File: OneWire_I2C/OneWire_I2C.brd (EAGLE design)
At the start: 22.2 x 28.2 mm, 14 parts, among them Q1 TP0602N3

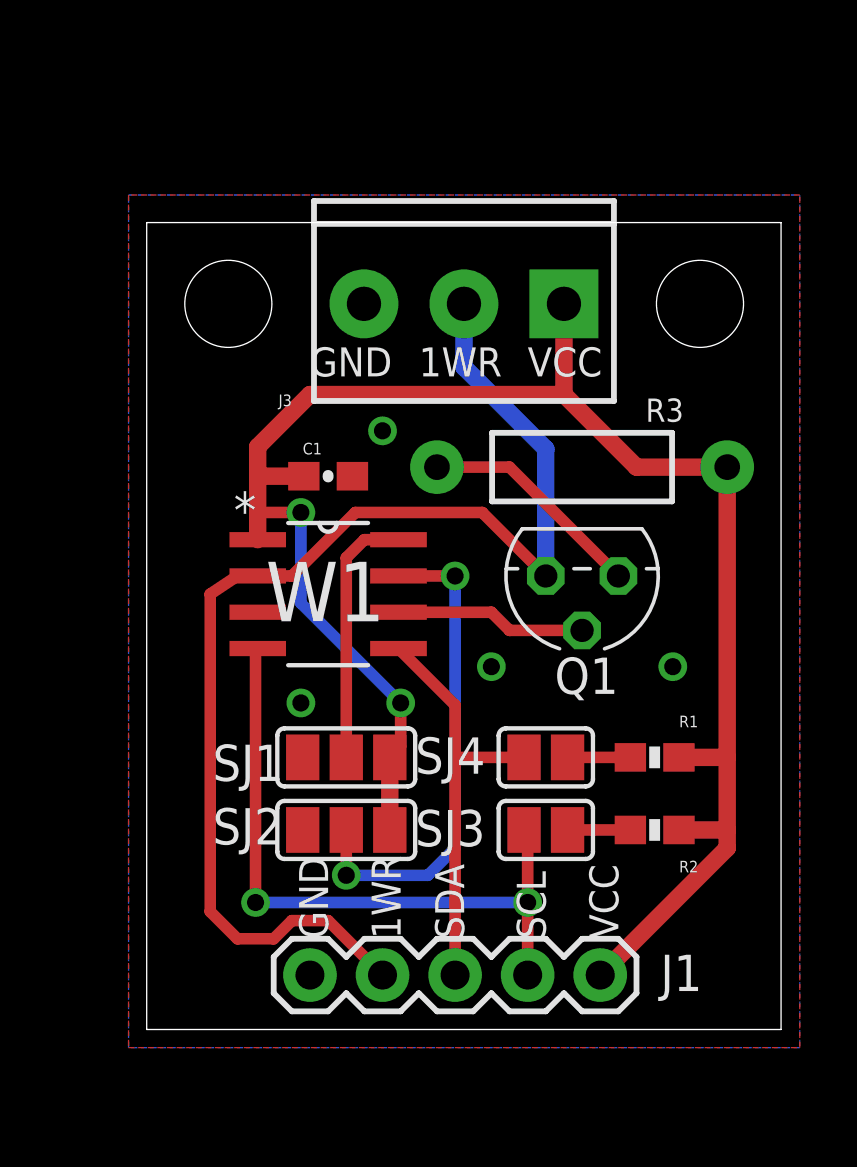
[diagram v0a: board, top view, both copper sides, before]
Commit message: Tweaks to I2C 1Wire bridge boards
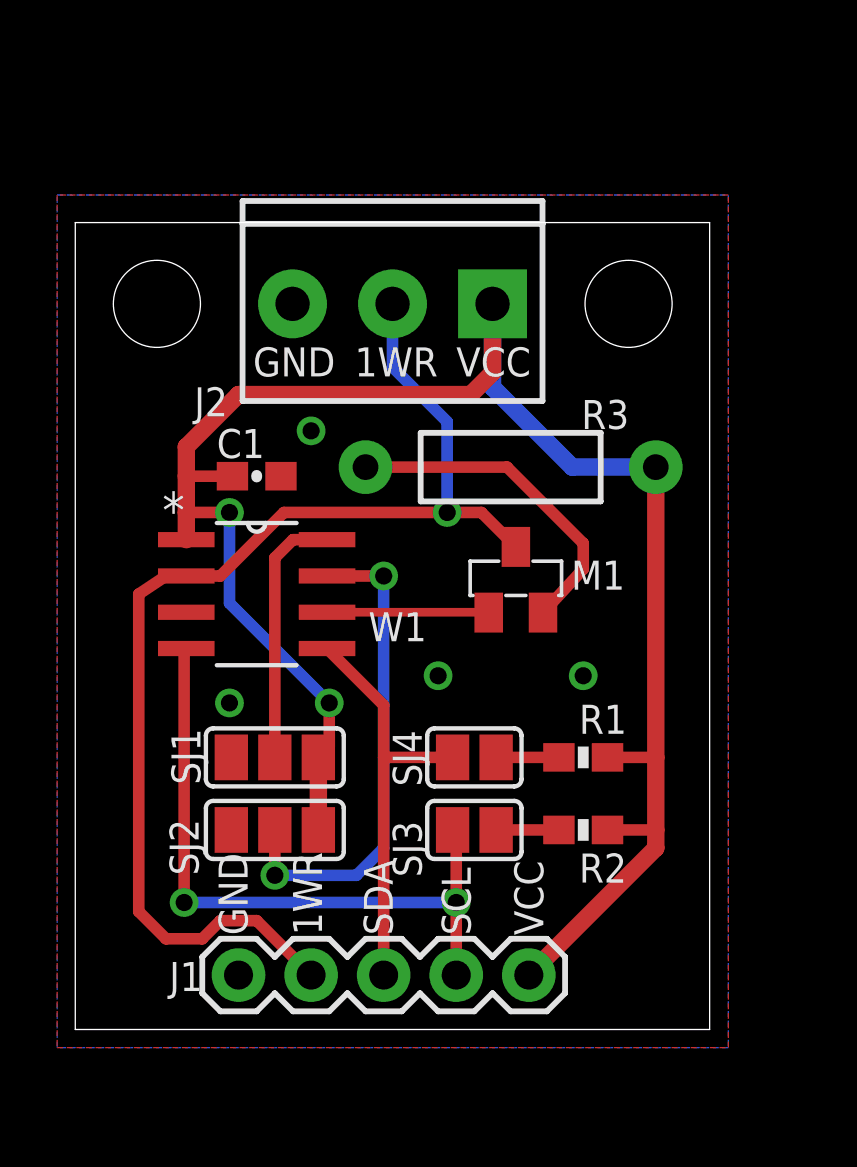
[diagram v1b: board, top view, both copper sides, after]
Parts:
- removed J3: (no value), SparkFun-Connectors:SCREWTERMINAL-3.5MM-3
- removed Q1: TP0602N3, transistor-fet:TO-92
- added J2: (no value), SparkFun-Connectors:SCREWTERMINAL-3.5MM-3
- added M1: BSS84, Puffin:SOT-23
- moved R3 2.50 mm to (15.3, 19.7)
- moved SJ3 2.50 mm to (14.0, 6.99)
- moved SJ4 2.50 mm to (14.0, 9.53)
- moved C1 2.50 mm to (6.39, 19.4)
- moved W1 2.50 mm to (6.39, 15.2)
- moved J1 2.50 mm to (15.9, 1.91)
- moved R1 2.50 mm to (17.8, 9.53)
- moved R2 2.50 mm to (17.8, 6.99)
- moved SJ1 2.50 mm to (7.03, 9.53)
- moved SJ2 2.50 mm to (7.03, 6.99)
- moved U$1 2.50 mm to (2.90, 25.4)
- moved U$2 2.50 mm to (19.4, 25.4)
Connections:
- removed net PCTL: Q1.2, W1.6
- new net N$1: M1.1, W1.6
- net 1WR: now also J2.2, M1.3; no longer J3.2, Q1.3
- net GND: now also J2.3; no longer J3.3
- net N$10: now also M1.2; no longer Q1.1
- net VCC: now also J2.1; no longer J3.1
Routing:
- net PCTL: track 6.69 -> 0.00 mm
- net N$1: track 0.00 -> 5.67 mm
- net N$10: track 7.93 -> 11.7 mm
- net VCC: track 63.5 -> 66.1 mm
- net 1WR: track 42.4 -> 40.8 mm, vias 0 -> 1

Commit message: Changed I2C pullup jumpers to single 3-way jumper
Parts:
- removed SJ4: (no value), jumper:SJ
- SJ3: device jumper:SJ -> jumper:SJ_2
- moved SJ3 4.74 mm to (18.5, 8.50), turned to 90 degrees
- moved R2 3.54 mm to (14.3, 7.49)
- moved R1 3.50 mm to (14.3, 9.53)
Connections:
- removed net N$4: R1.2, SJ4.2
- new net N$2: R1.1, SJ3.3
- net N$3: now also R2.1, SJ3.1; no longer R2.2, SJ3.2
- net SCL: now also R2.2; no longer SJ3.1
- net SDA: now also R1.2; no longer SJ4.1
- net VCC: now also SJ3.2; no longer R1.1, R2.1
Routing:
- net N$2: track 0.00 -> 3.56 mm
- net N$4: track 2.20 -> 0.00 mm
- net N$3: track 2.20 -> 3.54 mm
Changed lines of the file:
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@@
 <setting verticaltext="up"/>
 </settings>
-<grid distance="0.5" unitdist="mm" unit="mm" style="dots" multiple="1" display="yes" altdistance="0.1" altunitdist="mm" altunit="mm"/>
+<grid distance="0.01" unitdist="inch" unit="inch" style="dots" multiple="1" display="yes" altdistance="0.005" altunitdist="inch" altunit="inch"/>
 <layers>
-<layer number="1" name="Top" color="4" fill="1" visible="no" active="yes"/>
+<layer number="1" name="Top" color="4" fill="1" visible="yes" active="yes"/>
 <layer number="2" name="Route2" color="1" fill="3" visible="no" active="no"/>
 <layer number="3" name="Route3" color="4" fill="3" visible="no" active="no"/>
@@
 <attribute name="VALUE" x="5.374" y="18.2245" size="0.4064" layer="27" font="vector"/>
 </element>
-<element name="R1" library="SparkFun-Resistors" package="0603-RES" value="" x="17.82" y="9.525" smashed="yes" rot="R180">
-<attribute name="NAME" x="19.344" y="11.3665" size="1.016" layer="25" font="vector" ratio="15" rot="R180"/>
-<attribute name="VALUE" x="18.836" y="10.668" size="0.4064" layer="27" font="vector" rot="R180"/>
-</element>
-<element name="R2" library="SparkFun-Resistors" package="0603-RES" value="" x="17.82" y="6.985" smashed="yes" rot="R180">
-<attribute name="NAME" x="19.344" y="6.1595" size="1.016" layer="25" font="vector" ratio="15" rot="R180"/>
-<attribute name="VALUE" x="18.836" y="8.128" size="0.4064" layer="27" font="vector" rot="R180"/>
-</element>
-<element name="SJ3" library="jumper" package="SJ" value="" x="14.01" y="6.985" smashed="yes">
-<attribute name="NAME" x="12.1685" y="5.334" size="1.016" layer="25" font="vector" ratio="15" rot="R90"/>
-<attribute name="VALUE" x="14.4101" y="6.985" size="0.02" layer="27"/>
-</element>
-<element name="SJ4" library="jumper" package="SJ" value="" x="14.01" y="9.525" smashed="yes">
-<attribute name="NAME" x="12.1685" y="8.509" size="1.016" layer="25" font="vector" ratio="15" rot="R90"/>
-<attribute name="VALUE" x="14.4101" y="9.525" size="0.02" layer="27"/>
+<element name="R1" library="SparkFun-Resistors" package="0603-RES" value="" x="14.32" y="9.525" smashed="yes" rot="R180">
+<attribute name="NAME" x="12.844" y="10.1665" size="1.016" layer="25" font="vector" ratio="15" rot="R180"/>
+<attribute name="VALUE" x="15.336" y="10.668" size="0.4064" layer="27" font="vector" rot="R180"/>
+</element>
+<element name="R2" library="SparkFun-Resistors" package="0603-RES" value="" x="14.32" y="7.485" smashed="yes" rot="R180">
+<attribute name="NAME" x="12.744" y="8.1595" size="1.016" layer="25" font="vector" ratio="15" rot="R180"/>
+<attribute name="VALUE" x="15.336" y="8.628" size="0.4064" layer="27" font="vector" rot="R180"/>
 </element>
 <element name="SJ2" library="jumper" package="SJ_2" value="" x="7.025" y="6.985" smashed="yes" rot="R180">
@@
 <attribute name="NAME" x="17.3995" y="15.3955" size="1.016" layer="25" font="vector" ratio="15"/>
 </element>
+<element name="SJ3" library="jumper" package="SJ_2" value="" x="18.5" y="8.5" smashed="yes" rot="R90">
+<attribute name="NAME" x="20.73" y="7.325" size="1.016" layer="25" font="vector" ratio="15" rot="R90"/>
+<attribute name="VALUE" x="18.5" y="8.3999" size="0.02" layer="27" rot="R90"/>
+</element>
 </elements>
 <signals>
 <signal name="VCC">
-<contactref element="R1" pad="1"/>
-<contactref element="R2" pad="1"/>
 <contactref element="W1" pad="1"/>
 <contactref element="C1" pad="1"/>
@@
 <contactref element="J1" pad="1"/>
 <contactref element="J2" pad="1"/>
-<wire x1="15.915" y1="1.905" x2="20.36" y2="6.35" width="0.6096" layer="1"/>
-<wire x1="20.36" y1="6.35" x2="20.36" y2="6.985" width="0.6096" layer="1"/>
-<wire x1="20.36" y1="6.985" x2="20.36" y2="9.525" width="0.6096" layer="1"/>
-<wire x1="20.36" y1="9.525" x2="20.36" y2="19.685" width="0.6096" layer="1"/>
-<wire x1="18.67" y1="9.525" x2="20.36" y2="9.525" width="0.4064" layer="1"/>
-<wire x1="18.67" y1="6.985" x2="20.36" y2="6.985" width="0.4064" layer="1"/>
-<wire x1="3.9262" y1="17.145" x2="3.9262" y2="18.0975" width="0.6096" layer="1"/>
-<wire x1="3.9262" y1="18.0975" x2="3.9262" y2="19.3675" width="0.6096" layer="1"/>
+<wire x1="20.36" y1="4.35" x2="20.36" y2="8.5" width="0.6096" layer="1"/>
+<wire x1="20.36" y1="8.5" x2="20.36" y2="19.685" width="0.6096" layer="1"/>
+<wire x1="3.9262" y1="17.145" x2="3.9262" y2="19.3675" width="0.6096" layer="1"/>
 <wire x1="3.9262" y1="19.3675" x2="3.9262" y2="20.3962" width="0.6096" layer="1"/>
 <wire x1="3.9262" y1="20.3962" x2="5.755" y2="22.225" width="0.6096" layer="1"/>
@@
 <wire x1="8.93" y1="9.906" x2="8.93" y2="11.43" width="0.4064" layer="1"/>
 <via x="8.93" y="11.43" extent="1-16" drill="0.6"/>
-<wire x1="8.93" y1="11.43" x2="5.4375" y2="14.9225" width="0.4064" layer="16"/>
-<wire x1="5.4375" y1="14.9225" x2="5.4375" y2="18.0975" width="0.4064" layer="16"/>
-<via x="5.4375" y="18.0975" extent="1-16" drill="0.6"/>
-<wire x1="5.4375" y1="18.0975" x2="3.9262" y2="18.0975" width="0.4064" layer="1"/>
+<wire x1="8.93" y1="11.43" x2="3.9135" y2="16.4465" width="0.4064" layer="16"/>
+<wire x1="3.9135" y1="16.4465" x2="3.9135" y2="19.3675" width="0.4064" layer="16"/>
+<via x="3.9135" y="19.3675" extent="1-16" drill="0.6"/>
 <wire x1="20.36" y1="19.685" x2="17.439" y2="19.685" width="0.6096" layer="16"/>
 <wire x1="17.439" y1="19.685" x2="14.645" y2="22.479" width="0.6096" layer="16"/>
@@
 <wire x1="13.883" y1="22.225" x2="14.645" y2="22.987" width="0.6096" layer="1"/>
 <wire x1="14.645" y1="22.987" x2="14.645" y2="25.4" width="0.6096" layer="1"/>
+<contactref element="SJ3" pad="2"/>
+<wire x1="18.5" y1="8.5" x2="20.36" y2="8.5" width="0.4064" layer="1"/>
+<wire x1="20.36" y1="4.35" x2="20.35" y2="4.35" width="0.6096" layer="1"/>
+<wire x1="20.35" y1="4.35" x2="18" y2="2" width="0.6096" layer="1"/>
+<wire x1="18" y1="2" x2="16.01" y2="2" width="0.6096" layer="1"/>
+<wire x1="16.01" y1="2" x2="15.915" y2="1.905" width="0.6096" layer="1"/>
+<wire x1="3.9135" y1="19.3675" x2="3.9262" y2="19.3675" width="0" layer="19" extent="1-1"/>
 </signal>
 <signal name="GND">
@@
 <via x="5.4375" y="11.43" extent="1-16" drill="0.6"/>
 </signal>
-<signal name="N$3">
-<contactref element="SJ3" pad="2"/>
-<contactref element="R2" pad="2"/>
-<wire x1="14.772" y1="6.985" x2="16.97" y2="6.985" width="0.4064" layer="1"/>
-</signal>
-<signal name="N$4">
-<contactref element="SJ4" pad="2"/>
-<contactref element="R1" pad="2"/>
-<wire x1="14.772" y1="9.525" x2="16.97" y2="9.525" width="0.4064" layer="1"/>
-</signal>
 <signal name="SCL">
 <contactref element="W1" pad="4"/>
-<contactref element="SJ3" pad="1"/>
 <contactref element="J1" pad="2"/>
 <wire x1="3.9262" y1="13.335" x2="3.85" y2="13.335" width="0.4064" layer="1"/>
@@
 <via x="13.375" y="4.445" extent="1-16" drill="0.6"/>
 <wire x1="13.375" y1="4.445" x2="13.375" y2="1.905" width="0.4064" layer="1"/>
-<wire x1="13.248" y1="6.985" x2="13.375" y2="6.985" width="0.4064" layer="1"/>
 <wire x1="13.375" y1="6.985" x2="13.375" y2="4.445" width="0.4064" layer="1"/>
+<contactref element="R2" pad="2"/>
+<wire x1="13.375" y1="6.985" x2="13.47" y2="7.485" width="0" layer="19" extent="1-1"/>
 </signal>
 <signal name="AD1">
@@
 <signal name="SDA">
 <contactref element="W1" pad="5"/>
-<contactref element="SJ4" pad="1"/>
 <contactref element="J1" pad="3"/>
-<wire x1="10.835" y1="1.905" x2="10.835" y2="9.525" width="0.4064" layer="1"/>
+<wire x1="10.835" y1="1.905" x2="10.835" y2="9.5" width="0.4064" layer="1"/>
 <wire x1="10.835" y1="9.525" x2="10.835" y2="11.3538" width="0.4064" layer="1"/>
 <wire x1="10.835" y1="11.3538" x2="8.8538" y2="13.335" width="0.4064" layer="1"/>
-<wire x1="13.248" y1="9.525" x2="10.835" y2="9.525" width="0.4064" layer="1"/>
+<contactref element="R1" pad="2"/>
+<wire x1="13.47" y1="9.525" x2="10.835" y2="9.525" width="0.4064" layer="1"/>
+<wire x1="10.835" y1="9.525" x2="10.835" y2="9.5" width="0.4064" layer="1"/>
 </signal>
 <signal name="1WR">
@@
 <wire x1="14.5125" y1="14.605" x2="14.5125" y2="14.5925" width="0.4064" layer="1"/>
 </signal>
+<signal name="N$2">
+<contactref element="R1" pad="1"/>
+<contactref element="SJ3" pad="3"/>
+<wire x1="18.5" y1="10.024" x2="17.024" y2="10.024" width="0.4064" layer="1"/>
+<wire x1="17.024" y1="10.024" x2="16.5" y2="9.5" width="0.4064" layer="1"/>
+<wire x1="16.5" y1="9.5" x2="15.195" y2="9.5" width="0.4064" layer="1"/>
+<wire x1="15.195" y1="9.5" x2="15.17" y2="9.525" width="0.4064" layer="1"/>
+</signal>
+<signal name="N$3">
+<contactref element="R2" pad="1"/>
+<contactref element="SJ3" pad="1"/>
+<wire x1="15.17" y1="7.485" x2="16.515" y2="7.485" width="0.4064" layer="1"/>
+<wire x1="16.515" y1="7.485" x2="17" y2="7" width="0.4064" layer="1"/>
+<wire x1="17" y1="7" x2="18.476" y2="7" width="0.4064" layer="1"/>
+<wire x1="18.476" y1="7" x2="18.5" y2="6.976" width="0.4064" layer="1"/>
+</signal>
 </signals>

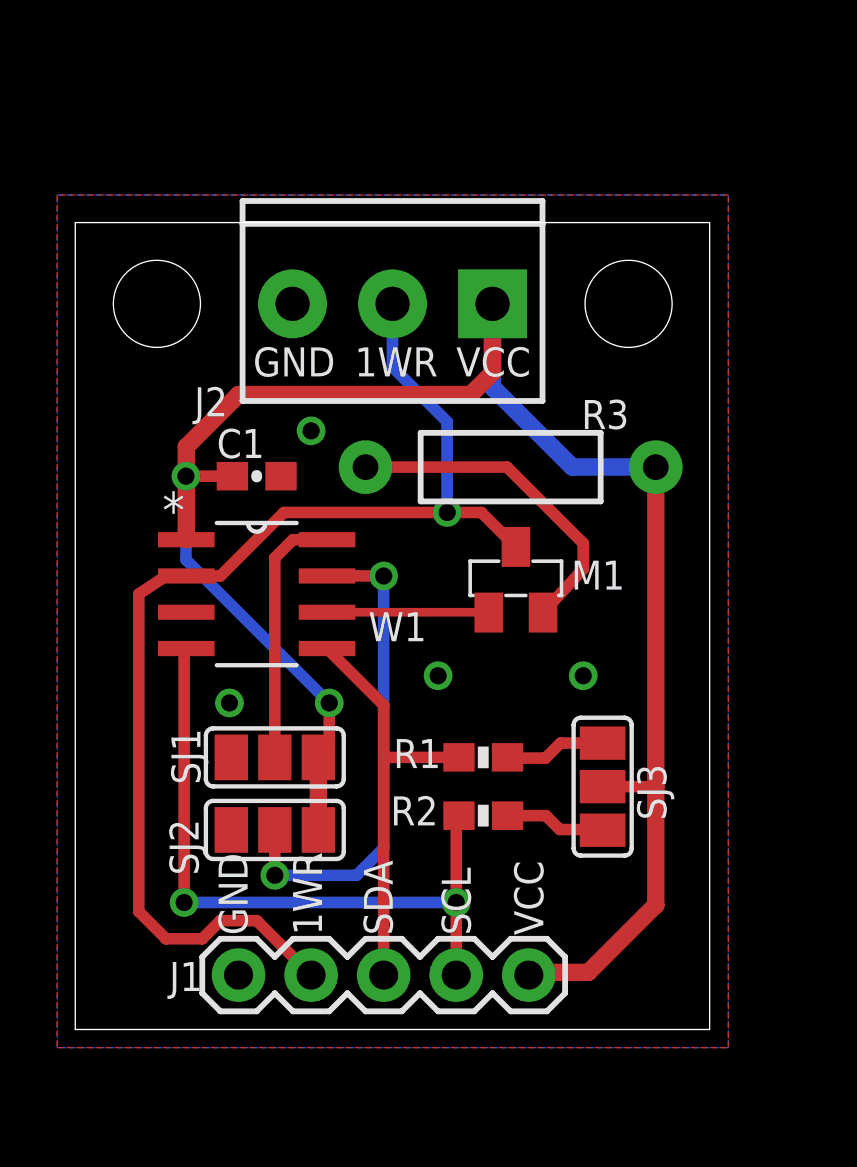
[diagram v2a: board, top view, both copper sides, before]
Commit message: Added extra screw terminals on I2C side
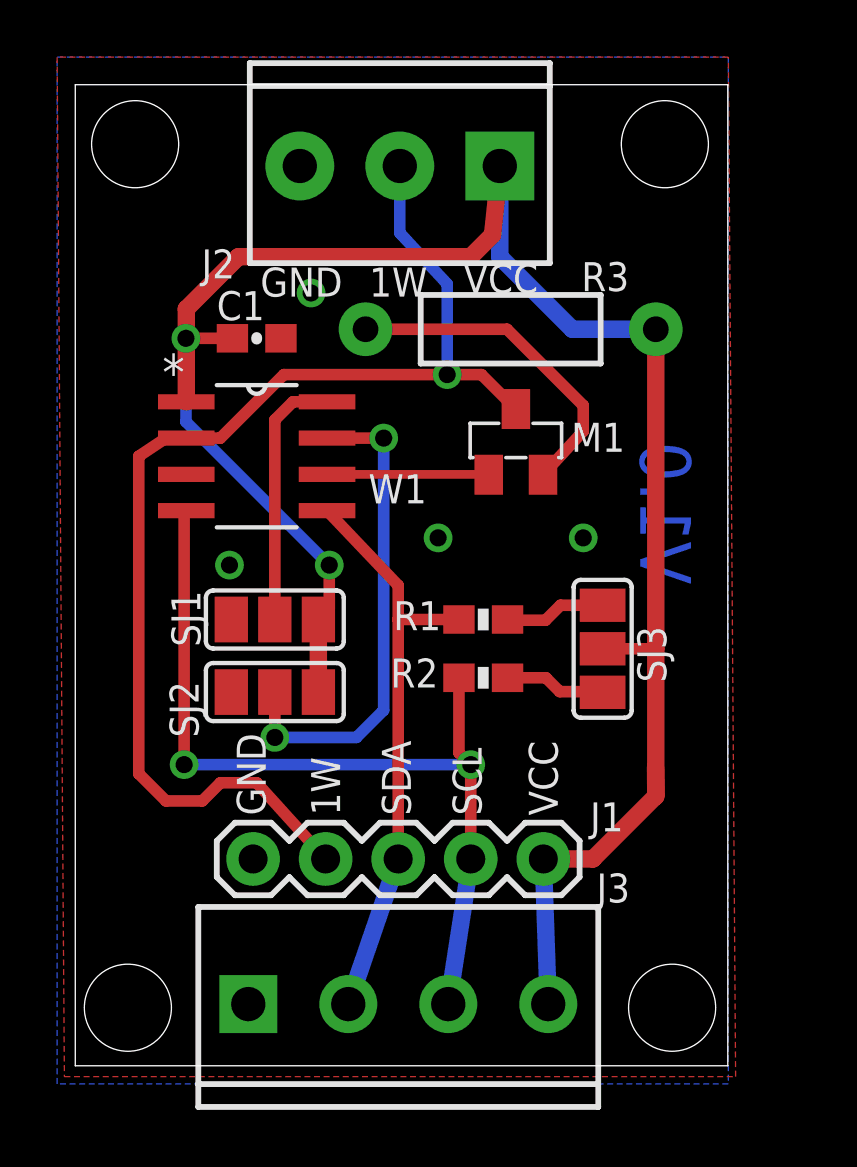
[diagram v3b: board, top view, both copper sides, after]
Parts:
- added J3: (no value), SparkFun-Connectors:SCREWTERMINAL-3.5MM-4
- added U$3, U$4: (no value), SparkFun-Electromechanical:STAND-OFF-TIGHT
- moved U$2 5.73 mm to (20.7, 31.0)
- moved U$1 5.64 mm to (2.14, 31.0)
- moved J2 4.83 mm to (14.9, 30.2)
- moved C1 4.83 mm to (6.39, 24.2)
- moved M1 4.83 mm to (15.0, 21.0)
- moved R1 4.83 mm to (14.3, 14.4)
- moved R3 4.83 mm to (15.3, 24.5)
- moved SJ1 4.83 mm to (7.03, 14.4)
- moved SJ3 4.83 mm to (18.5, 13.3)
- moved R2 4.83 mm to (14.3, 12.3)
- moved SJ2 4.83 mm to (7.03, 11.8)
- moved W1 4.83 mm to (6.39, 20.1)
- moved J1 4.10 mm to (16.4, 5.97)
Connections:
- net GND: now also J3.1
- net SCL: now also J3.3
- net SDA: now also J3.2
- net VCC: now also J3.4
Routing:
- net SCL: track 23.6 -> 30.7 mm
- net VCC: track 66.1 -> 72.5 mm
- net SDA: track 14.9 -> 20.7 mm
- net 1WR: track 40.8 -> 41.5 mm
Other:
- board size 22.2 x 28.2 mm -> 22.8 x 34.3 mm
- board text added: "1W"
- board text added: "V1.0"
- board text removed: "1WR"
